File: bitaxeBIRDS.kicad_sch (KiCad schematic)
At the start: 10 parts, among them J1 XT30

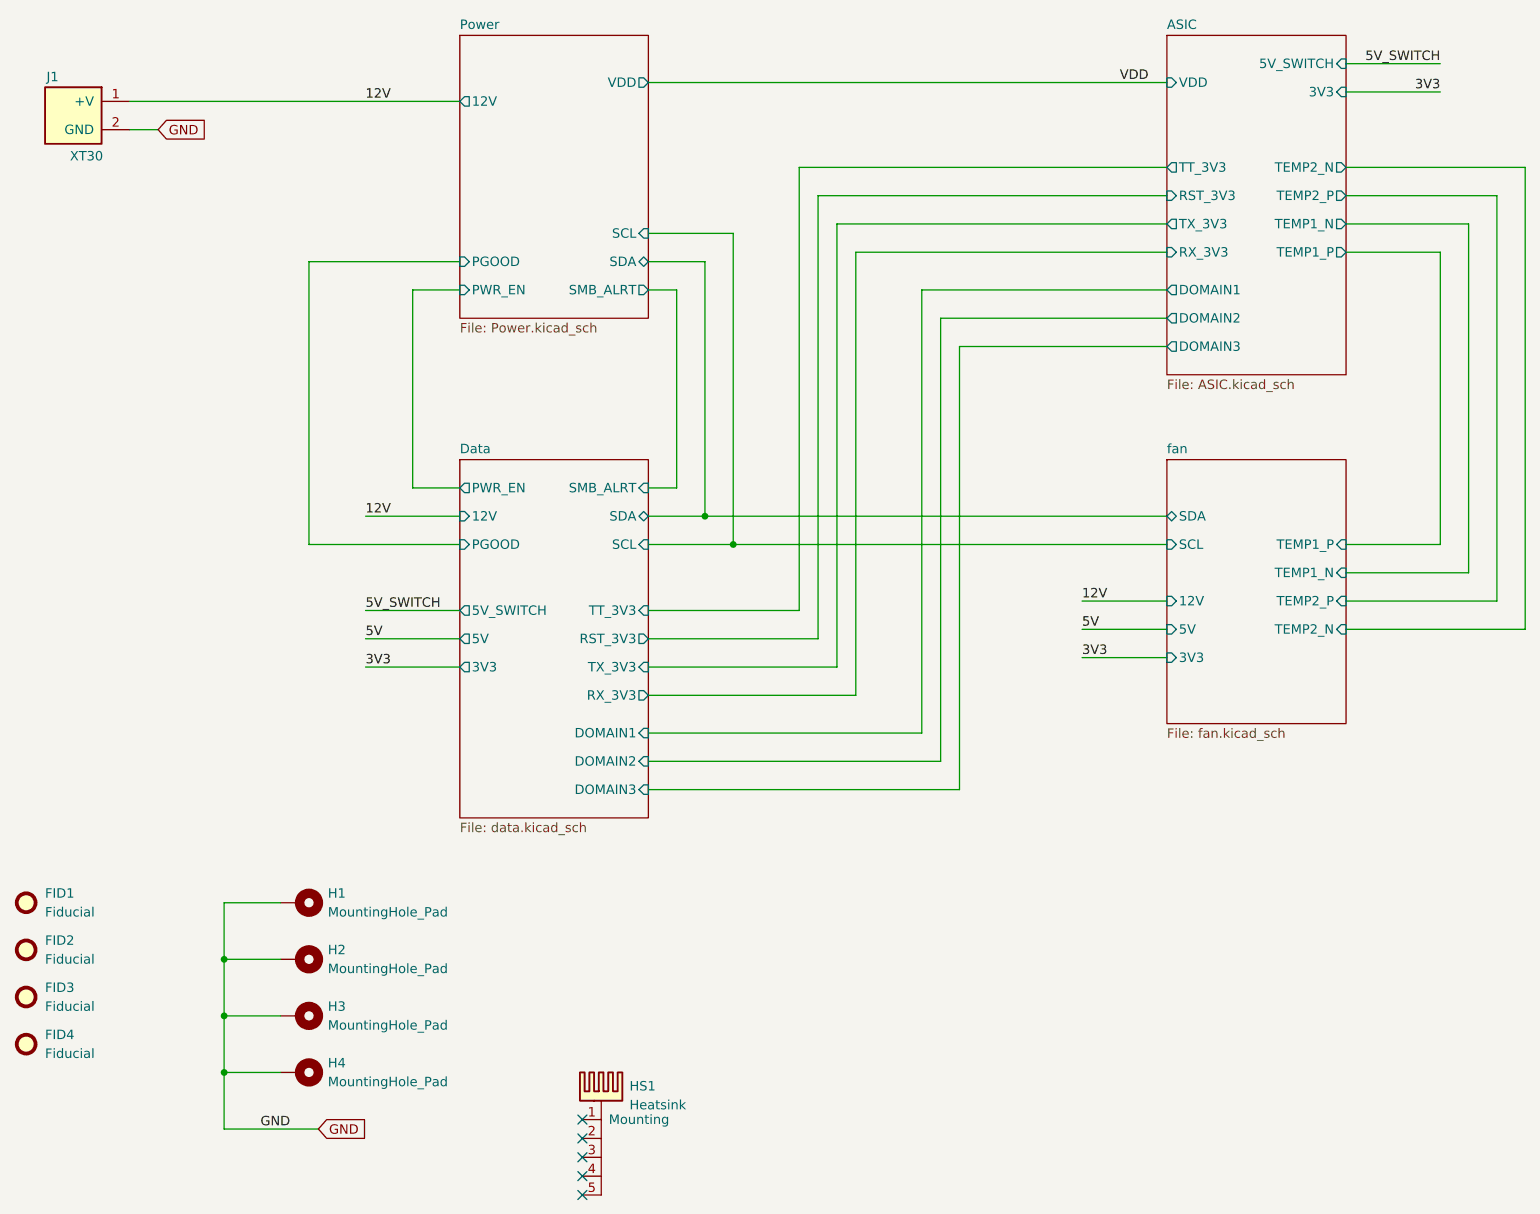
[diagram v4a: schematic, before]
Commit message: Removed EMC2103, added discrete fan control, DRC pass, fixed logo.
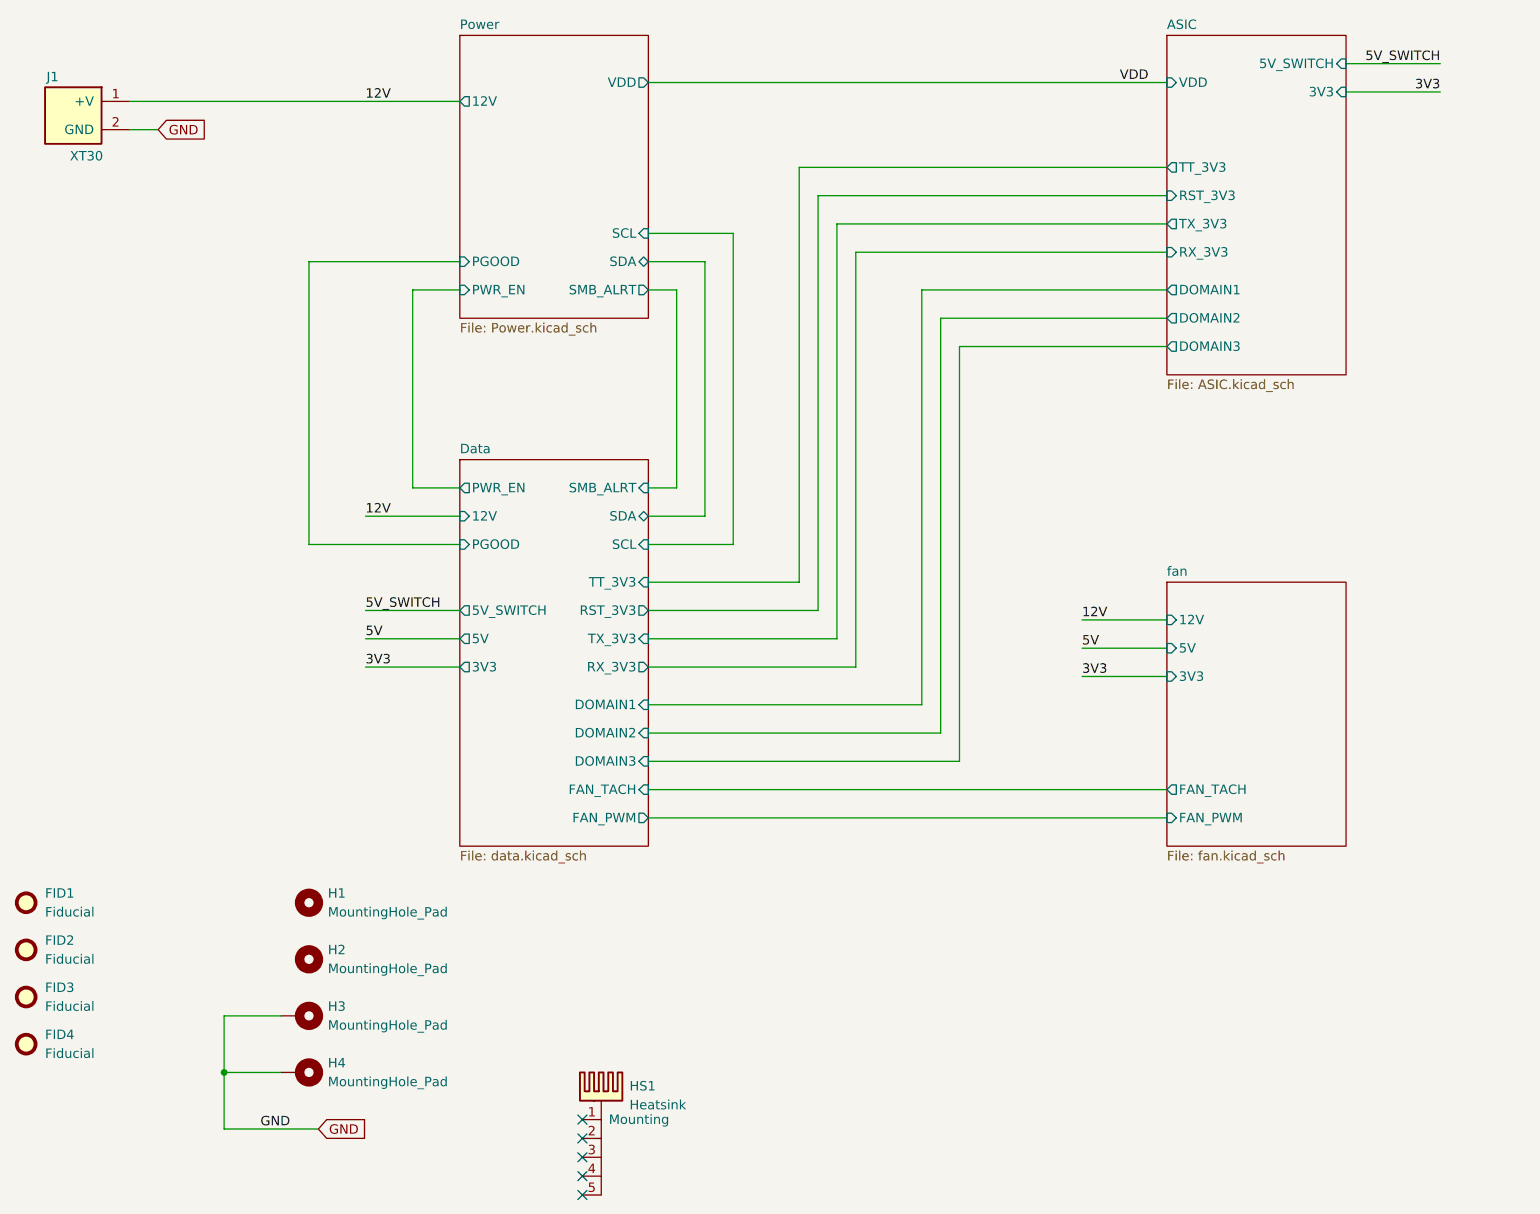
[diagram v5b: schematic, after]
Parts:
- H1, H2: footprint MountingHole:MountingHole_3.2mm_M3_Pad_Via -> MountingHole:MountingHole_3.2mm_M3; symbol Mechanical:MountingHole_Pad -> Mechanical:MountingHole
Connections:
- net GND: no longer H1.1, H2.1
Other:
- sheet ASIC ports: added none; removed TEMP1_N, TEMP1_P, TEMP2_N, TEMP2_P
- sheet Data ports: added FAN_PWM, FAN_TACH; removed none
- sheet fan ports: added FAN_PWM, FAN_TACH; removed SCL, SDA, TEMP1_N, TEMP1_P, TEMP2_N, TEMP2_P

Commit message: clean up some of the schematic errors for #4
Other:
- sheet Data ports: added none; removed 12V
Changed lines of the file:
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@@
-	(wire
-		(pts
-			(xy 90.17 100.33) (xy 102.87 100.33)
-		)
-		(stroke
-			(width 0)
-			(type default)
-		)
-	)
 	(wire
 		(pts
@@
 	(label "12V"
 		(at 186.69 114.3 0)
-		(effects
-			(font
-				(size 1.27 1.27)
-			)
-			(justify left bottom)
-		)
-	)
-	(label "12V"
-		(at 90.17 100.33 0)
 		(effects
 			(font
@@
 			(effects
 				(font
-					(size 1.27 1.27)
-				)
-				(justify left)
-			)
-		)
-		(pin "12V" input
-			(at 102.87 100.33 180)
-			(effects
-				(font

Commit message: cleaned up lots of ERC errors and warnings for #4
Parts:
- HS1: footprint bitaxe:Heatsink-5hole-BitaxeGT -> bitaxe:Heatsink-BitaxeGT
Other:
- sheet ASIC ports: added TRIP_3V3; removed TT_3V3
- sheet Data ports: added TRIP_3V3; removed TT_3V3
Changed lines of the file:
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@@
 			)
 		)
-		(property "Footprint" "bitaxe:Heatsink-5hole-BitaxeGT"
+		(property "Footprint" "bitaxe:Heatsink-BitaxeGT"
 			(at 122.2248 179.07 0)
 			(effects
@@
 			)
 		)
-		(pin "TT_3V3" input
+		(pin "TRIP_3V3" input
 			(at 128.27 109.22 0)
 			(effects
@@
 			)
 		)
-		(pin "TT_3V3" output
+		(pin "TRIP_3V3" output
 			(at 198.12 53.34 180)
 			(effects
